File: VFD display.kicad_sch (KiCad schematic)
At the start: 39 parts

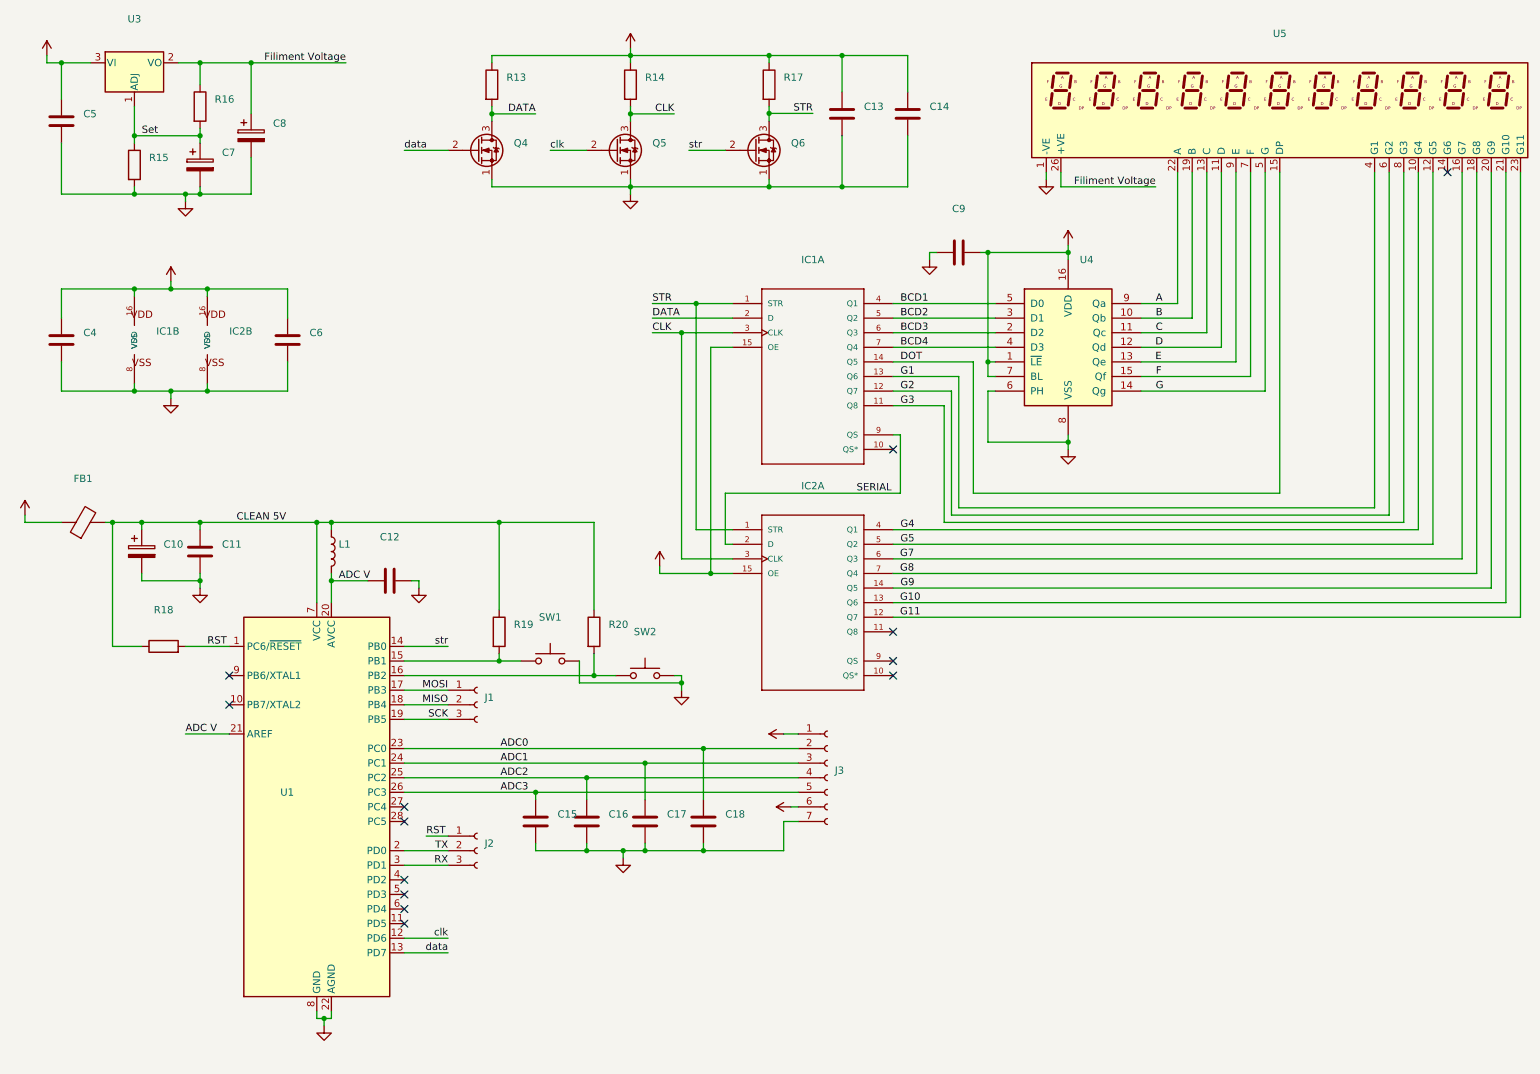
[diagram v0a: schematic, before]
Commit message: V2 Schematic updates added indication LEDs for 12V and 5V, fixed the display symbol so C is connected to pin 17, added values to the capacitors on the ADC lines, removed voltage from AREF.
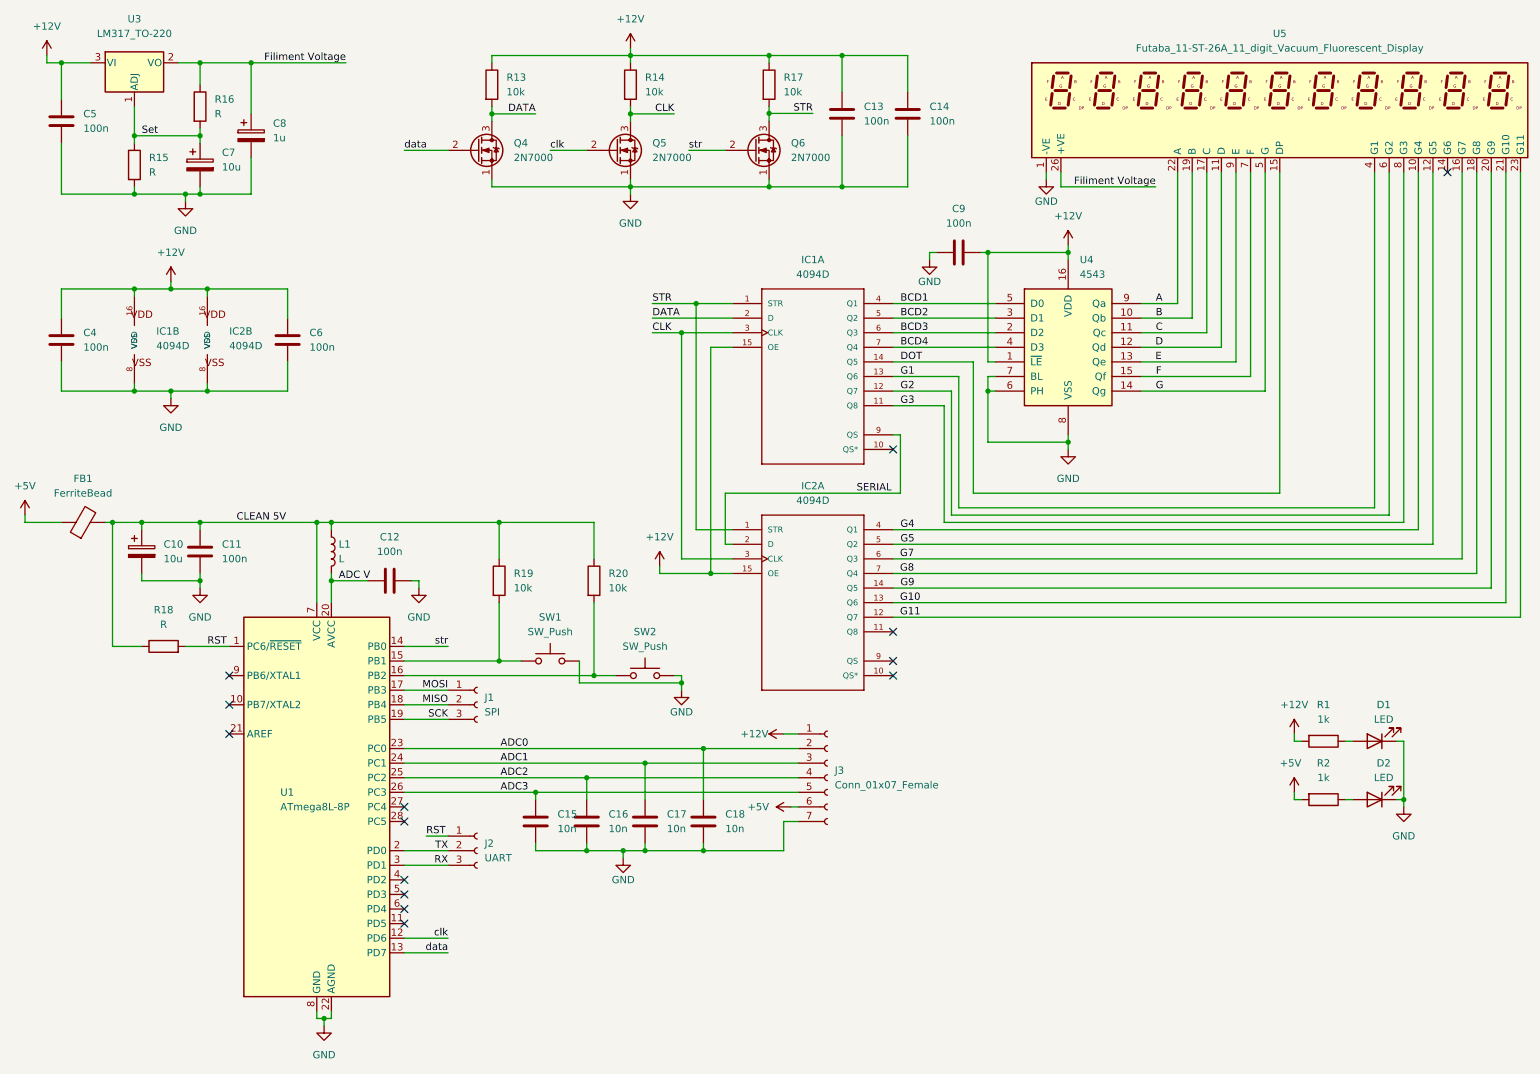
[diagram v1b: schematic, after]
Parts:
- added D1, D2: LED, symbol Device:LED
- added R1, R2: 1k, symbol Device:R
- C10, C7: value (none) -> 10u; footprint (none) -> Capacitor_THT:CP_Radial_D5.0mm_P2.00mm
- C11, C12, C13, C14, C4, C5, C6, C9: value (none) -> 100n; footprint (none) -> Capacitor_THT:C_Disc_D3.4mm_W2.1mm_P2.50mm
- C15, C16, C17: value (none) -> 10n; footprint (none) -> Capacitor_THT:C_Disc_D4.7mm_W2.5mm_P5.00mm
- C18: value (none) -> 10n; footprint (none) -> Capacitor_THT:C_Disc_D3.4mm_W2.1mm_P2.50mm
- C8: value (none) -> 1u; footprint (none) -> Capacitor_THT:CP_Radial_D5.0mm_P2.00mm
- FB1: value (none) -> FerriteBead; footprint (none) -> Inductor_SMD:L_0603_1608Metric_Pad1.05x0.95mm_HandSolder
- IC1, IC2: value (none) -> 4094D; footprint (none) -> Package_DIP:DIP-16_W7.62mm_LongPads
- J1: value (none) -> SPI; footprint (none) -> Connector_PinSocket_2.54mm:PinSocket_1x03_P2.54mm_Vertical
- J2: value (none) -> UART; footprint (none) -> Connector_PinSocket_2.54mm:PinSocket_1x03_P2.54mm_Vertical
- J3: value (none) -> Conn_01x07_Female; footprint (none) -> Connector_PinSocket_2.54mm:PinSocket_1x07_P2.54mm_Vertical
- L1: value (none) -> L; footprint (none) -> Inductor_SMD:L_0603_1608Metric_Pad1.05x0.95mm_HandSolder
- Q4, Q5, Q6: value (none) -> 2N7000; footprint (none) -> Package_TO_SOT_THT:TO-92_Inline_Wide
- R13, R14, R17, R19, R20: value (none) -> 10k; footprint (none) -> Resistor_THT:R_Axial_DIN0207_L6.3mm_D2.5mm_P2.54mm_Vertical
- R15, R16, R18: value (none) -> R; footprint (none) -> Resistor_THT:R_Axial_DIN0207_L6.3mm_D2.5mm_P2.54mm_Vertical
- SW1, SW2: value (none) -> SW_Push; footprint (none) -> Button_Switch_THT:SW_PUSH_6mm
- U1: value (none) -> ATmega8L-8P; footprint (none) -> Package_DIP:DIP-28_W7.62mm_LongPads
- U3: value (none) -> LM317_TO-220
- U4: value (none) -> 4543; footprint (none) -> Package_DIP:DIP-16_W7.62mm_LongPads
- U5: value (none) -> Futaba_11-ST-26A_11_digit_Vacuum_Fluorescent_Display; footprint (none) -> Connector_PinSocket_2.54mm:PinSocket_1x26_P2.54mm_Vertical
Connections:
- net +12V: now also R1.2; no longer U4.7 (BL)
- net +5V: now also R2.2
- net ADC V: no longer U1.21 (AREF)
- net C: now also U5.17 (C); no longer U5.13 (C)
- net GND: now also U4.7 (BL), D1.1 (K), D2.1 (K)
- new net: D2.2 (A), R2.1
- new net: D1.2 (A), R1.1
- no-connect marks 13 -> 14
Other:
- moved on the sheet: R19, R20
